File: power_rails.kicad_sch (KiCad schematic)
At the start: 31 parts, among them SW3 ~{SR}, SW4 ~{PB}, U12 MCP1799T-5002H/TT, U5 AP63200WU, U7 AP63205WU, U8 STM6601CM2DDM6F, U9 TPS62162DSG

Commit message: finalizing pcb
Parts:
- C18, C22, C25: LCSC C84416 -> C326595
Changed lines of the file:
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@@
 			)
 		)
-		(property "LCSC" "C84416"
+		(property "LCSC" "C326595"
 			(at 0 0 0)
 			(hide yes)
@@
 			)
 		)
-		(property "LCSC" "C84416"
+		(property "LCSC" "C326595"
 			(at 0 0 0)
 			(hide yes)
@@
 			)
 		)
-		(property "LCSC" "C84416"
-			(at 0 0 0)
-			(hide yes)
+		(property "LCSC" "C326595"
+			(at 0 0 0)
+			(hide yes)

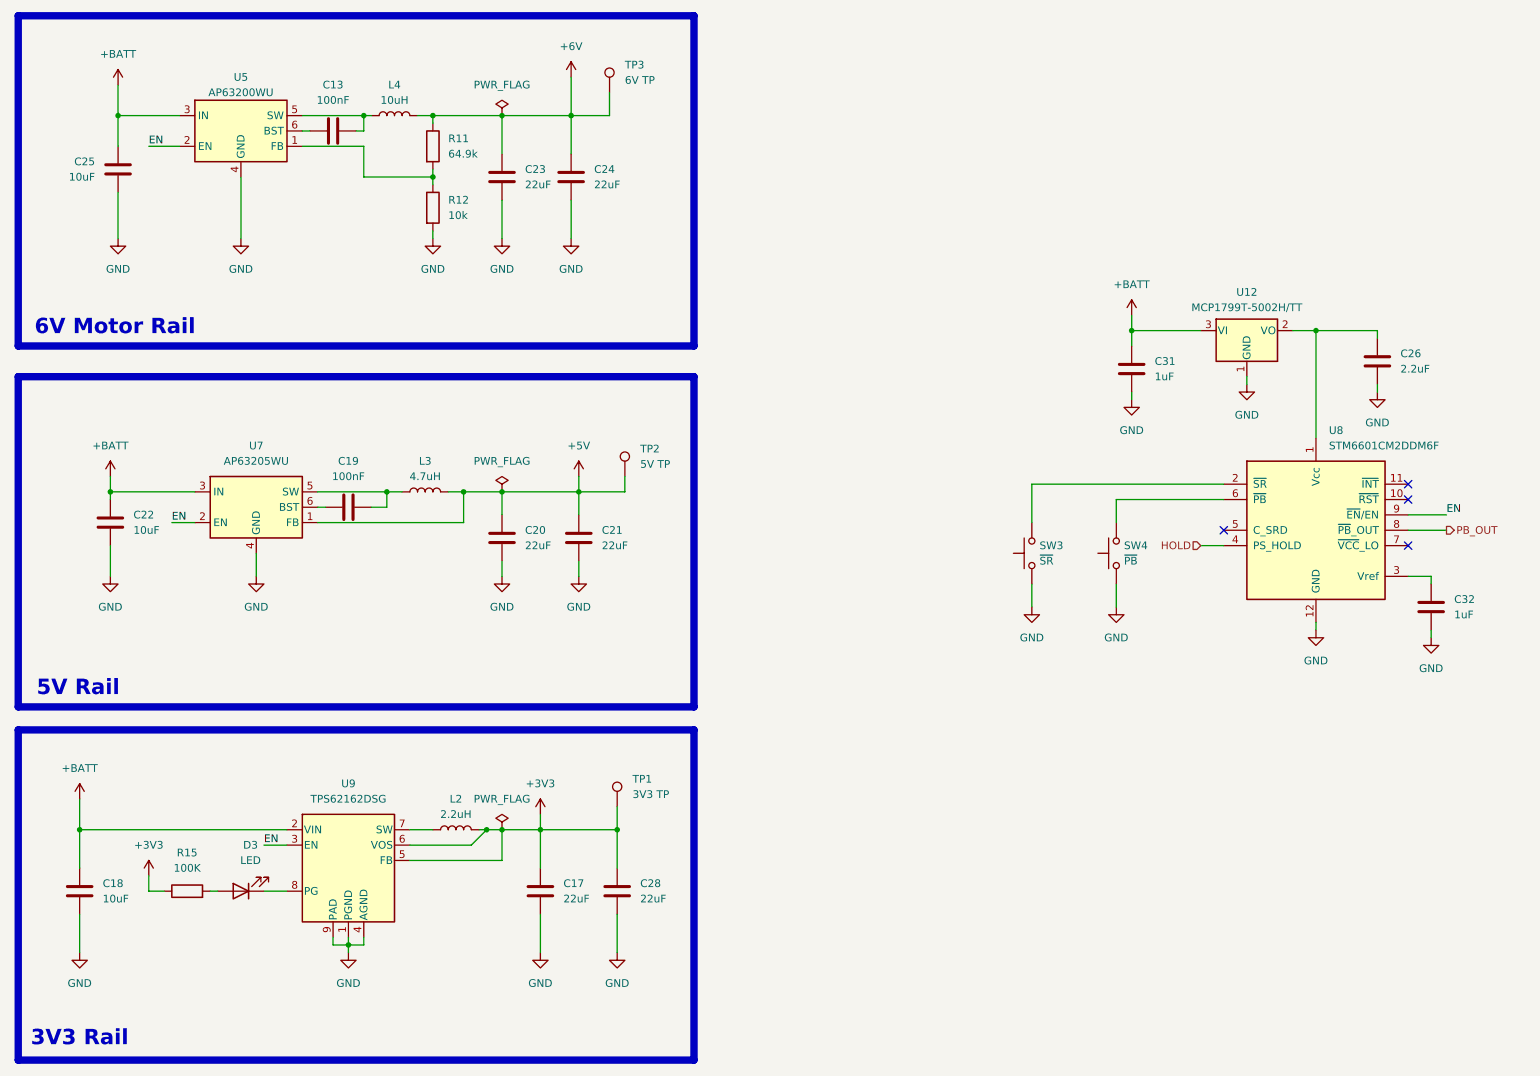
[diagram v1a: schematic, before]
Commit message: solve a problem with enable resistor and capacitor
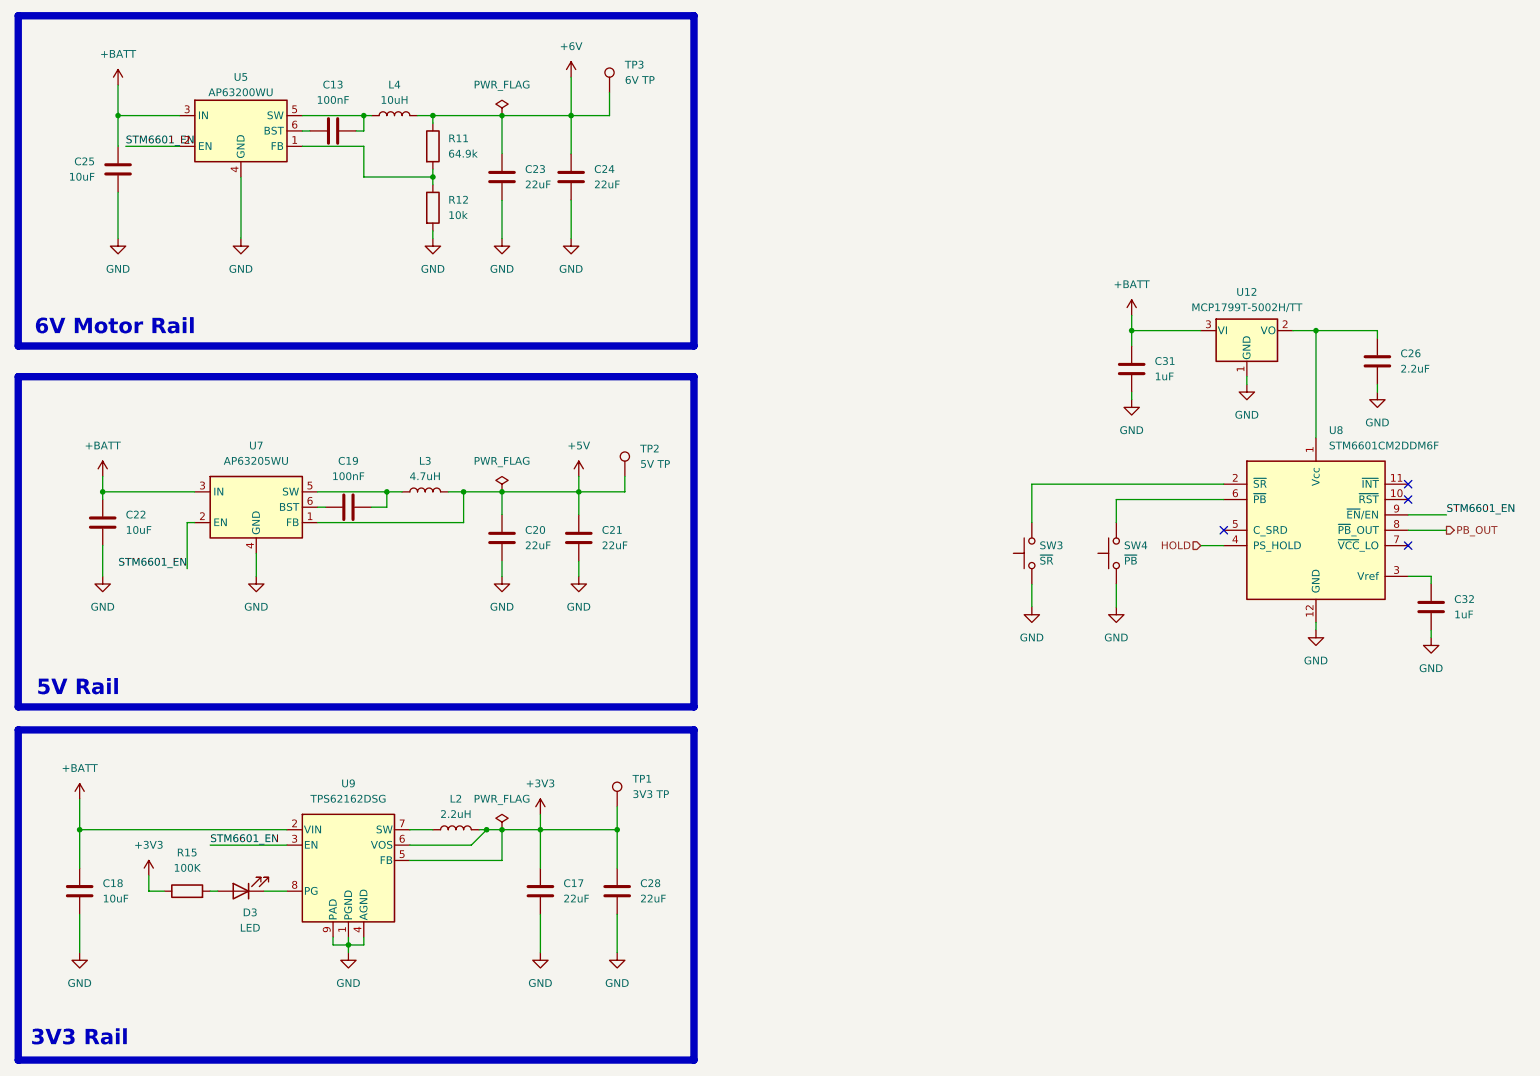
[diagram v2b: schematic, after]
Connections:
- net EN renamed STM6601_EN
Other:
- moved on the sheet: C22
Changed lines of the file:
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@@
 	)
 	(junction
-		(at 45.72 97.79)
+		(at 44.45 97.79)
 		(diameter 0)
 		(color 0 0 0 0)
@@
 	(wire
 		(pts
-			(xy 45.72 95.25) (xy 45.72 99.06)
+			(xy 44.45 95.25) (xy 44.45 99.06)
 		)
 		(stroke
@@
 	(wire
 		(pts
-			(xy 71.12 156.21) (xy 74.93 156.21)
+			(xy 62.23 156.21) (xy 74.93 156.21)
 		)
 		(stroke
@@
 	(wire
 		(pts
+			(xy 58.42 102.87) (xy 59.69 102.87)
+		)
+		(stroke
+			(width 0)
+			(type default)
+		)
+	)
+	(wire
+		(pts
 			(xy 106.68 153.67) (xy 107.95 153.67)
 		)
@@
 	(wire
 		(pts
+			(xy 58.42 110.49) (xy 58.42 102.87)
+		)
+		(stroke
+			(width 0)
+			(type default)
+		)
+	)
+	(wire
+		(pts
 			(xy 77.47 40.64) (xy 87.63 40.64)
 		)
@@
 	(wire
 		(pts
-			(xy 45.72 106.68) (xy 45.72 111.76)
+			(xy 44.45 106.68) (xy 44.45 111.76)
 		)
 		(stroke
@@
 	(wire
 		(pts
-			(xy 45.72 97.79) (xy 59.69 97.79)
+			(xy 44.45 97.79) (xy 59.69 97.79)
 		)
 		(stroke
@@
 	(wire
 		(pts
-			(xy 52.07 40.64) (xy 57.15 40.64)
+			(xy 48.26 40.64) (xy 57.15 40.64)
 		)
 		(stroke
@@
 	(wire
 		(pts
-			(xy 55.88 102.87) (xy 59.69 102.87)
-		)
-		(stroke
-			(width 0)
-			(type default)
-		)
-	)
-	(wire
-		(pts
 			(xy 52.07 161.29) (xy 52.07 163.83)
 		)
@@
 		)
 	)
-	(label "EN"
-		(at 52.07 40.64 0)
+	(label "STM6601_EN"
+		(at 48.26 40.64 0)
 		(effects
 			(font
@@
 		)
 	)
-	(label "EN"
-		(at 55.88 102.87 0)
+	(label "STM6601_EN"
+		(at 58.42 110.49 180)
 		(effects
 			(font
 				(size 1.27 1.27)
 			)
-			(justify left bottom)
+			(justify right bottom)
 		)
 	)
-	(label "EN"
-		(at 71.12 156.21 0)
+	(label "STM6601_EN"
+		(at 62.23 156.21 0)
 		(effects
 			(font
@@
 		)
 	)
-	(label "EN"
+	(label "STM6601_EN"
 		(at 266.7 101.6 0)
 		(effects
@@
 	(symbol
 		(lib_id "power:+BATT")
-		(at 45.72 95.25 0)
+		(at 44.45 95.25 0)
 		(unit 1)
 		(body_style 1)
@@
 		(fields_autoplaced yes)
 		(property "Reference" "#PWR059"
-			(at 45.72 99.06 0)
+			(at 44.45 99.06 0)
 			(hide yes)
 			(show_name no)
@@
 		)
 		(property "Value" "+BATT"
-			(at 45.72 90.17 0)
+			(at 44.45 90.17 0)
 			(show_name no)
 			(do_not_autoplace no)
@@
 		)
 		(property "Footprint" ""
-			(at 45.72 95.25 0)
+			(at 44.45 95.25 0)
 			(hide yes)
 			(show_name no)
@@
 		)
 		(property "Datasheet" ""
-			(at 45.72 95.25 0)
+			(at 44.45 95.25 0)
 			(hide yes)
 			(show_name no)
@@
 		)
 		(property "Description" "Power symbol creates a global label with name \"+BATT\""
-			(at 45.72 95.25 0)
+			(at 44.45 95.25 0)
 			(hide yes)
 			(show_name no)
@@
 	(symbol
 		(lib_id "power:GND")
-		(at 45.72 111.76 0)
+		(at 44.45 111.76 0)
 		(unit 1)
 		(body_style 1)
@@
 		(fields_autoplaced yes)
 		(property "Reference" "#PWR060"
-			(at 45.72 118.11 0)
+			(at 44.45 118.11 0)
 			(hide yes)
 			(show_name no)
@@
 		)
 		(property "Value" "GND"
-			(at 45.72 116.84 0)
+			(at 44.45 116.84 0)
 			(show_name no)
 			(do_not_autoplace no)
@@
 		)
 		(property "Footprint" ""
-			(at 45.72 111.76 0)
+			(at 44.45 111.76 0)
 			(hide yes)
 			(show_name no)
@@
 		)
 		(property "Datasheet" ""
-			(at 45.72 111.76 0)
+			(at 44.45 111.76 0)
 			(hide yes)
 			(show_name no)
@@
 		)
 		(property "Description" "Power symbol creates a global label with name \"GND\" , ground"
-			(at 45.72 111.76 0)
+			(at 44.45 111.76 0)
 			(hide yes)
 			(show_name no)
@@
 		(in_pos_files yes)
 		(dnp no)
-		(fields_autoplaced yes)
 		(property "Reference" "D3"
-			(at 68.8975 156.21 0)
+			(at 68.834 167.386 0)
 			(show_name no)
 			(do_not_autoplace no)
@@
 		)
 		(property "Value" "LED"
-			(at 68.8975 158.75 0)
+			(at 68.834 169.926 0)
 			(show_name no)
 			(do_not_autoplace no)
@@
 	(symbol
 		(lib_id "Device:C")
-		(at 45.72 102.87 0)
+		(at 44.45 102.87 0)
 		(unit 1)
 		(body_style 1)
@@
 		(fields_autoplaced yes)
 		(property "Reference" "C22"
-			(at 49.53 101.5999 0)
+			(at 48.26 101.5999 0)
 			(show_name no)
 			(do_not_autoplace no)
@@
 		)
 		(property "Value" "10uF"
-			(at 49.53 104.1399 0)
+			(at 48.26 104.1399 0)
 			(show_name no)
 			(do_not_autoplace no)
@@
 		)
 		(property "Footprint" "Capacitor_SMD:C_0805_2012Metric"
-			(at 46.6852 106.68 0)
+			(at 45.4152 106.68 0)
 			(hide yes)
 			(show_name no)
@@
 		)
 		(property "Datasheet" "https://datasheet.lcsc.com/datasheet/pdf/7bcffd7e105d4d878e7542545928cdd2.pdf?productCode=C84416"
-			(at 45.72 102.87 0)
+			(at 44.45 102.87 0)
 			(hide yes)
 			(show_name no)
@@
 		)
 		(property "Description" "Unpolarized capacitor"
-			(at 45.72 102.87 0)
+			(at 44.45 102.87 0)
 			(hide yes)
 			(show_name no)
@@
 		)
 		(property "Manufacturer" "Generic"
-			(at 0 0 0)
+			(at -1.27 0 0)
 			(hide yes)
 			(show_name no)
@@
 		)
 		(property "MPN" "GPC0805106"
-			(at 0 0 0)
+			(at -1.27 0 0)
 			(hide yes)
 			(show_name no)
@@
 		)
 		(property "LCSC" "C326595"
-			(at 0 0 0)
+			(at -1.27 0 0)
 			(hide yes)
 			(show_name no)

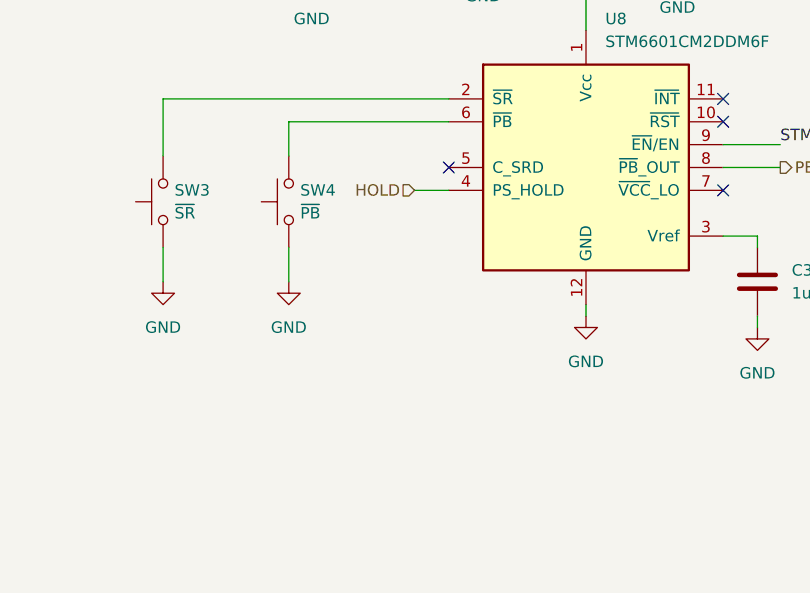
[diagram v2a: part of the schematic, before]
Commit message: fix: add capacitor to STM6601 for a ~5 seconds hard power off
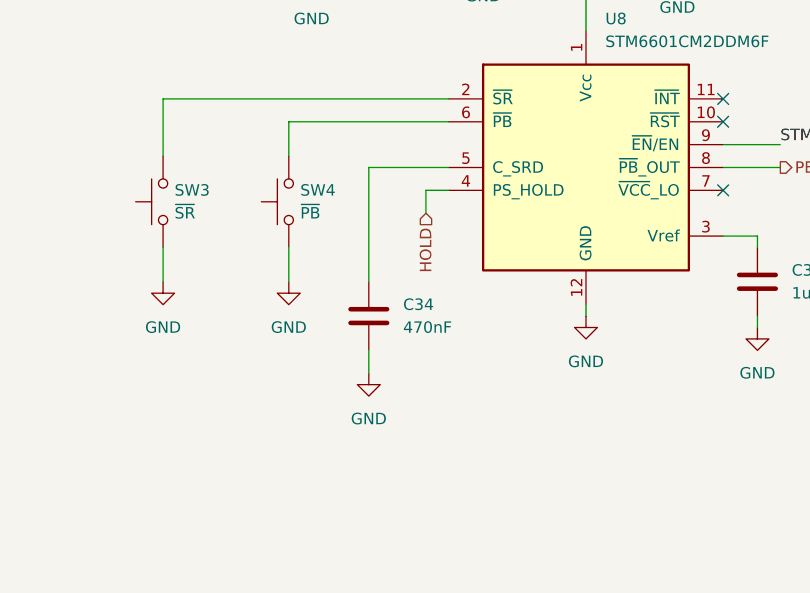
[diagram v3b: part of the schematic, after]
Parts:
- added C34: 470nF, Capacitor_SMD:C_0603_1608Metric, symbol Device:C
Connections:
- net GND: now also C34.2
- net at U8.5 (C_SRD): now also C34.1
- no-connect marks 4 -> 3
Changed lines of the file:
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@@
 		(at 260.35 106.68)
 	)
-	(no_connect
-		(at 229.87 104.14)
-	)
 	(wire
 		(pts
@@
 	(wire
 		(pts
+			(xy 227.33 106.68) (xy 229.87 106.68)
+		)
+		(stroke
+			(width 0)
+			(type default)
+		)
+	)
+	(wire
+		(pts
 			(xy 121.92 29.21) (xy 121.92 35.56)
 		)
@@
 	(wire
 		(pts
+			(xy 227.33 109.22) (xy 227.33 106.68)
+		)
+		(stroke
+			(width 0)
+			(type default)
+		)
+	)
+	(wire
+		(pts
 			(xy 87.63 40.64) (xy 87.63 45.72)
 		)
@@
 	(wire
 		(pts
-			(xy 226.06 106.68) (xy 229.87 106.68)
+			(xy 229.87 99.06) (xy 212.09 99.06)
 		)
 		(stroke
@@
 	(wire
 		(pts
-			(xy 229.87 99.06) (xy 212.09 99.06)
+			(xy 123.19 97.79) (xy 123.19 101.6)
 		)
 		(stroke
@@
 	(wire
 		(pts
-			(xy 123.19 97.79) (xy 123.19 101.6)
+			(xy 220.98 104.14) (xy 220.98 116.84)
 		)
 		(stroke
@@
 	(wire
 		(pts
+			(xy 220.98 124.46) (xy 220.98 127)
+		)
+		(stroke
+			(width 0)
+			(type default)
+		)
+	)
+	(wire
+		(pts
 			(xy 40.64 153.67) (xy 40.64 160.02)
 		)
@@
 	(wire
 		(pts
+			(xy 220.98 104.14) (xy 229.87 104.14)
+		)
+		(stroke
+			(width 0)
+			(type default)
+		)
+	)
+	(wire
+		(pts
 			(xy 99.06 54.61) (xy 99.06 55.88)
 		)
@@
 	(hierarchical_label "HOLD"
 		(shape input)
-		(at 226.06 106.68 180)
+		(at 227.33 109.22 270)
 		(effects
 			(font
@@
 	(symbol
 		(lib_id "power:GND")
+		(at 220.98 127 0)
+		(unit 1)
+		(body_style 1)
+		(exclude_from_sim no)
+		(in_bom yes)
+		(on_board yes)
+		(in_pos_files yes)
+		(dnp no)
+		(fields_autoplaced yes)
+		(property "Reference" "#PWR096"
+			(at 220.98 133.35 0)
+			(hide yes)
+			(show_name no)
+			(do_not_autoplace no)
+			(effects
+				(font
+					(size 1.27 1.27)
+				)
+			)
+		)
+		(property "Value" "GND"
+			(at 220.98 132.08 0)
+			(show_name no)
+			(do_not_autoplace no)
+			(effects
+				(font
+					(size 1.27 1.27)
+				)
+			)
+		)
+		(property "Footprint" ""
+			(at 220.98 127 0)
+			(hide yes)
+			(show_name no)
+			(do_not_autoplace no)
+			(effects
+				(font
+					(size 1.27 1.27)
+				)
+			)
+		)
+		(property "Datasheet" ""
+			(at 220.98 127 0)
+			(hide yes)
+			(show_name no)
+			(do_not_autoplace no)
+			(effects
+				(font
+					(size 1.27 1.27)
+				)
+			)
+		)
+		(property "Description" "Power symbol creates a global label with name \"GND\" , ground"
+			(at 220.98 127 0)
+			(hide yes)
+			(show_name no)
+			(do_not_autoplace no)
+			(effects
+				(font
+					(size 1.27 1.27)
+				)
+			)
+		)
+		(pin "1"
+		)
+		(instances
+			(project "rover-circuit"
+				(path "/0461baee-3b25-4e1a-a5c1-d76b4b99c66c/f4b194fd-8f48-4986-9deb-ce512b0299fe"
+					(reference "#PWR096")
+					(unit 1)
+				)
+			)
+		)
+	)
+	(symbol
+		(lib_id "power:GND")
 		(at 198.12 116.84 0)
 		(unit 1)
@@
 					(unit 1)
 				)
+			)
+		)
+	)
+	(symbol
+		(lib_id "Device:C")
+		(at 220.98 120.65 0)
+		(unit 1)
+		(body_style 1)
+		(exclude_from_sim no)
+		(in_bom yes)
+		(on_board yes)
+		(in_pos_files yes)
+		(dnp no)
+		(fields_autoplaced yes)
+		(property "Reference" "C34"
+			(at 224.79 119.3799 0)
+			(show_name no)
+			(do_not_autoplace no)
+			(effects
+				(font
+					(size 1.27 1.27)
+				)
+				(justify left)
+			)
+		)
+		(property "Value" "470nF"
+			(at 224.79 121.9199 0)
+			(show_name no)
+			(do_not_autoplace no)
+			(effects
+				(font
+					(size 1.27 1.27)
+				)
+				(justify left)
+			)
+		)
+		(property "Footprint" "Capacitor_SMD:C_0603_1608Metric"
+			(at 221.9452 124.46 0)
+			(hide yes)
+			(show_name no)
+			(do_not_autoplace no)
+			(effects
+				(font
+					(size 1.27 1.27)
+				)
+			)
+		)
+		(property "Datasheet" "https://datasheet.lcsc.com/datasheet/pdf/02336ea48ea44ca18c72517dd3cb7b47.pdf?productCode=C5673"
+			(at 220.98 120.65 0)
+			(hide yes)
+			(show_name no)
+			(do_not_autoplace no)
+			(effects
+				(font
+					(size 1.27 1.27)
+				)
+			)
+		)
+		(property "Description" "Unpolarized capacitor"
+			(at 220.98 120.65 0)
+			(hide yes)
+			(show_name no)
+			(do_not_autoplace no)
+			(effects
+				(font
+					(size 1.27 1.27)
+				)
+			)
+		)
+		(property "LCSC" "C1623"
+			(at -43.18 3.81 0)
+			(hide yes)
+			(show_name no)
+			(do_not_autoplace no)
+			(effects
+				(font
+					(size 1.27 1.27)
+				)
+			)
+		)
+		(property "MPN" ""
+			(at -43.18 3.81 0)
+			(hide yes)
+			(show_name no)
+			(do_not_autoplace no)
+			(effects
+				(font
+					(size 1.27 1.27)
+				)
+			)
+		)
+		(property "Manufacturer" "Generic"
+			(at -43.18 3.81 0)
+			(hide yes)
+			(show_name no)
+			(do_not_autoplace no)
+			(effects
+				(font
+					(size 1.27 1.27)
+				)
+			)
+		)
+		(pin "1"
+		)
+		(pin "2"
+		)
+		(instances
+			(project "rover-circuit"
+				(path "/0461baee-3b25-4e1a-a5c1-d76b4b99c66c/f4b194fd-8f48-4986-9deb-ce512b0299fe"
+					(reference "C34")
+					(unit 1)
+				)
